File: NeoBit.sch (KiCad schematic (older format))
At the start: 19 parts, among them J1 AudioJack3_Ground, J2 Barrel_Jack_MountingPin, J3 Qwiic, J4 DotStars, J5 microbit_edge_connector, J6 NeoPixels, U1 74AHCT125, U2 MCP1702-3302E_TO92, U3 MCP1702-5002E_TO92

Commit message: Part numbers for terminal blocks.
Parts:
- J4: Description (none) -> TERM BLOCK 4POS SIDE ENT 3.5MM; Digi-Key_PN (none) -> A98038-ND; MPN (none) -> 1776275-4
- J6: Description (none) -> TERM BLOCK 3POS SIDE ENT 3.5MM; Digi-Key_PN (none) -> A98037-ND; MPN (none) -> 1776275-3
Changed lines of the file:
@@
 F 2 "footprints:TerminalBlock_4Ucon_1x03_P3.50mm_Vertical" H 6500 4800 50  0001 C CNN
 F 3 "" H 6500 4800 50  0001 C CNN
+F 4 "1776275-3" H 6500 4800 60  0001 C CNN "MPN"
+F 5 "TERM BLOCK 3POS SIDE ENT 3.5MM" H 6500 4800 60  0001 C CNN "Description"
+F 6 "A98037-ND" H 6500 4800 60  0001 C CNN "Digi-Key_PN"
 	1    6500 4800
 	1    0    0    -1
@@
 F 2 "footprints:TerminalBlock_4Ucon_1x04_P3.50mm_Vertical" H 5600 1600 50  0001 C CNN
 F 3 "" H 5600 1600 50  0001 C CNN
+F 4 "1776275-4" H 5600 1600 60  0001 C CNN "MPN"
+F 5 "TERM BLOCK 4POS SIDE ENT 3.5MM" H 5600 1600 60  0001 C CNN "Description"
+F 6 "A98038-ND" H 5600 1600 60  0001 C CNN "Digi-Key_PN"
 	1    5600 1600
 	1    0    0    -1

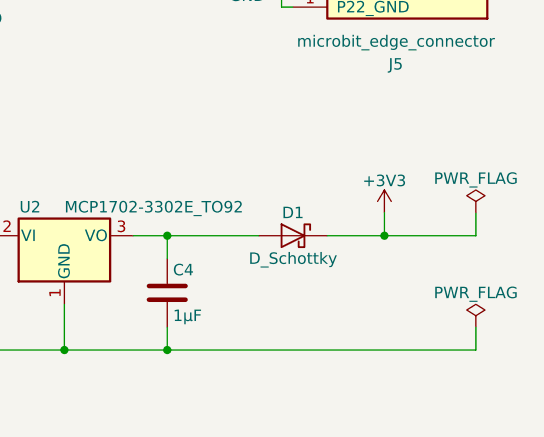
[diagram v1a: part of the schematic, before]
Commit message: Add 47uF capacitor on 3V3 supply.
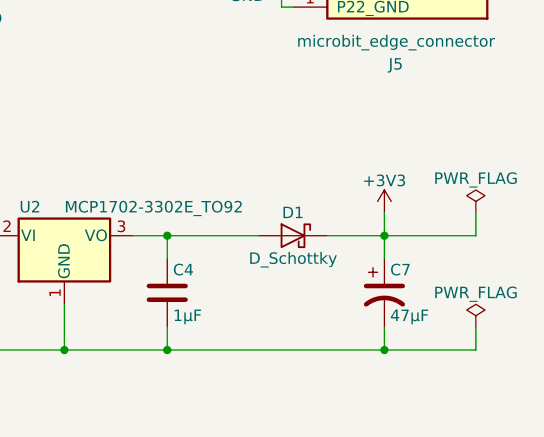
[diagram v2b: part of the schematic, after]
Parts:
- added C7: 47µF, Capacitors_THT:CP_Radial_D6.3mm_P2.50mm, symbol CP1
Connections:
- net +3V3: now also C7.1
- net GND: now also C7.2
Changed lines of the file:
@@
 NoConn ~ 7200 3500
 Wire Wire Line
-	7600 6000 7600 6100
+	7600 6000 7600 6200
 $Comp
 L +VDC #PWR018
@@
 Wire Wire Line
 	5100 4900 5350 4900
+$Comp
+L CP1 C7
+U 1 1 5B87C55E
+P 7600 6350
+F 0 "C7" H 7625 6450 50  0000 L CNN
+F 1 "47µF" H 7625 6250 50  0000 L CNN
+F 2 "Capacitors_THT:CP_Radial_D6.3mm_P2.50mm" H 7638 6200 50  0001 C CNN
+F 3 "" H 7600 6350 50  0001 C CNN
+F 4 "ECE-A1CKS470" H 7600 6350 60  0001 C CNN "MPN"
+F 5 "CAP ALUM 47UF 20% 16V RADIAL" H 7600 6350 60  0001 C CNN "Description"
+F 6 "P969-ND" H 7600 6350 60  0001 C CNN "Digi-Key_PN"
+	1    7600 6350
+	1    0    0    -1
+$EndComp
+Wire Wire Line
+	7600 6500 7600 6600
+Connection ~ 7600 6600
 $EndSCHEMATC

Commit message: Metadata.
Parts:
- J3: Description (none) -> Qwiic JST Connector - SMD 4-pin; MPN (none) -> PRT-14417
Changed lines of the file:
@@
 F 2 "Connectors_JST:JST_SH_SM04B-SRSS-TB_04x1.00mm_Angled" H 3900 1600 50  0001 C CNN
 F 3 "" H 3900 1600 50  0001 C CNN
+F 4 "PRT-14417" H 3900 1600 60  0001 C CNN "MPN"
+F 5 "Qwiic JST Connector - SMD 4-pin" H 3900 1600 60  0001 C CNN "Description"
 	1    3900 1600
 	1    0    0    -1

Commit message: Use new footprint for micro:bit edge connector.
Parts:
- J5: footprint footprints:4UCON_10156_90deg -> footprints:4UCON_10156_2x40_P1.27mm_Socket_Horizontal
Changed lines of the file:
@@
 F 0 "J5" H 7750 5350 50  0000 C CNN
 F 1 "microbit_edge_connector" H 7750 5250 50  0000 C CNN
-F 2 "footprints:4UCON_10156_90deg" H 7600 3200 50  0001 C CNN
+F 2 "footprints:4UCON_10156_2x40_P1.27mm_Socket_Horizontal" H 7600 3200 50  0001 C CNN
 F 3 "" H 7600 3200 50  0001 C CNN
 F 4 "3342" H 7700 3300 60  0001 C CNN "MPN"

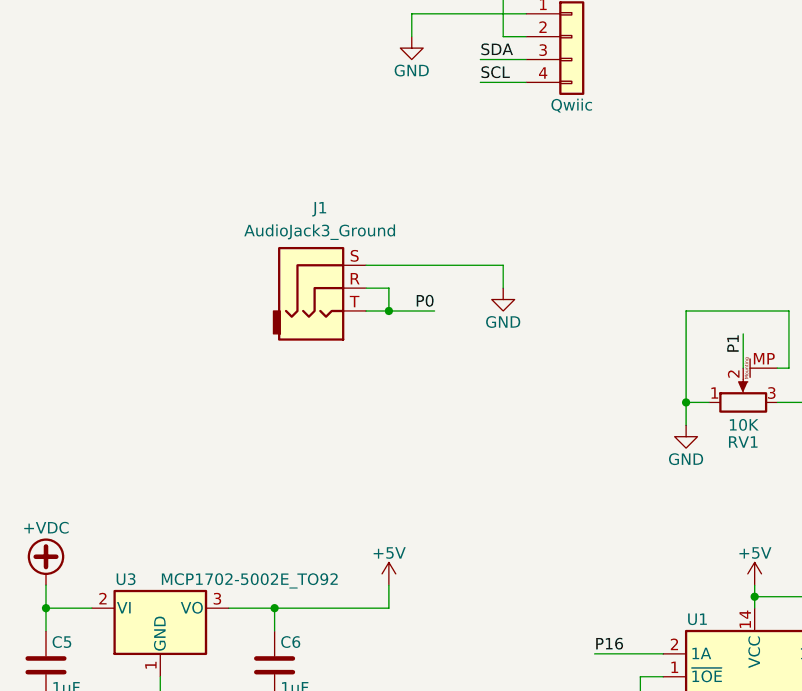
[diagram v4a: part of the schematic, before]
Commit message: Add filter to audio output.
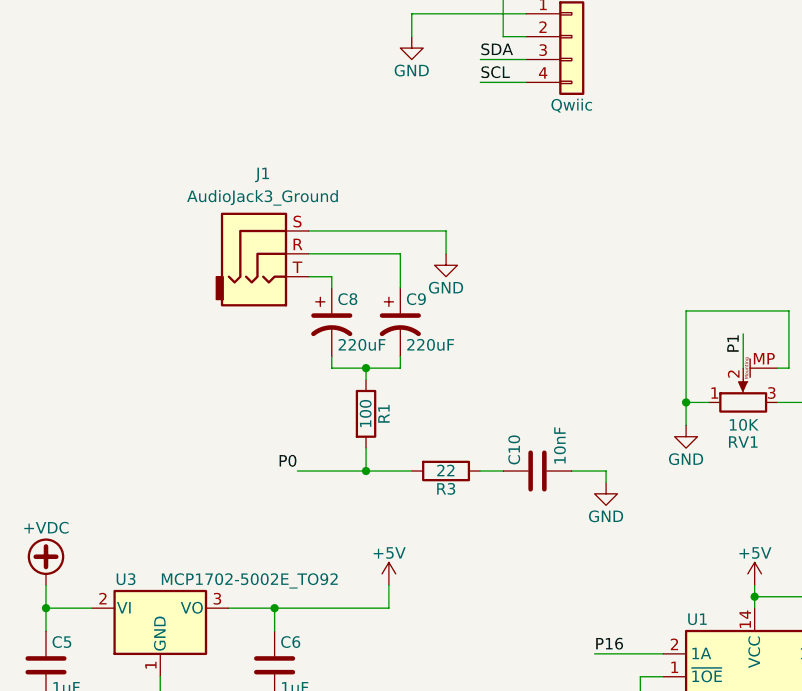
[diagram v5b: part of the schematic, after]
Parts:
- added C10: 10nF, Capacitors_THT:C_Disc_D3.8mm_W2.6mm_P2.50mm, symbol C
- added C8, C9: 220uF, Capacitors_THT:CP_Radial_D5.0mm_P2.50mm, symbol CP1
- added R1: 100, Resistors_THT:R_Axial_DIN0207_L6.3mm_D2.5mm_P2.54mm_Vertical, symbol R
- added R3: 22, Resistors_THT:R_Axial_DIN0207_L6.3mm_D2.5mm_P2.54mm_Vertical, symbol R
- R2: footprint Resistors_THT:R_Axial_DIN0207_L6.3mm_D2.5mm_P7.62mm_Horizontal -> Resistors_THT:R_Axial_DIN0207_L6.3mm_D2.5mm_P2.54mm_Vertical
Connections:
- net GND: now also C10.2
- net P0: now also R1.2, R3.2; no longer J1.R, J1.T
- new net: C9.1, J1.R
- new net: C8.1, J1.T
- new net: C8.2, C9.2, R1.1
- new net: C10.1, R3.1
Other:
- moved on the sheet: J1
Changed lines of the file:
@@
 F 0 "R2" V 5580 4550 50  0000 C CNN
 F 1 "470" V 5500 4550 50  0000 C CNN
-F 2 "Resistors_THT:R_Axial_DIN0207_L6.3mm_D2.5mm_P7.62mm_Horizontal" V 5430 4550 50  0001 C CNN
+F 2 "Resistors_THT:R_Axial_DIN0207_L6.3mm_D2.5mm_P2.54mm_Vertical" V 5430 4550 50  0001 C CNN
 F 3 "" H 5500 4550 50  0001 C CNN
 F 4 "CF14JT470R" H 5500 4550 60  0001 C CNN "MPN"
@@
 L AudioJack3_Ground J1
 U 1 1 5BA405B2
-P 2800 2700
-F 0 "J1" H 2800 3050 50  0000 C CNN
-F 1 "AudioJack3_Ground" H 2800 2950 50  0000 C CNN
-F 2 "footprints:SJ1-3533NG" H 2800 2700 50  0001 C CNN
-F 3 "" H 2800 2700 50  0001 C CNN
-F 4 "SJ1-3533NG" H 2800 2700 60  0001 C CNN "MPN"
-F 5 "CONN JACK STEREO 3.5MM R/A" H 2800 2700 60  0001 C CNN "Description"
-F 6 "CP1-3533NG-ND" H 2800 2700 60  0001 C CNN "Digi-Key_PN"
-	1    2800 2700
+P 2550 2550
+F 0 "J1" H 2550 2900 50  0000 C CNN
+F 1 "AudioJack3_Ground" H 2550 2800 50  0000 C CNN
+F 2 "footprints:SJ1-3533NG" H 2550 2550 50  0001 C CNN
+F 3 "" H 2550 2550 50  0001 C CNN
+F 4 "SJ1-3533NG" H 2550 2550 60  0001 C CNN "MPN"
+F 5 "CONN JACK STEREO 3.5MM R/A" H 2550 2550 60  0001 C CNN "Description"
+F 6 "CP1-3533NG-ND" H 2550 2550 60  0001 C CNN "Digi-Key_PN"
+	1    2550 2550
 	1    0    0    -1
 $EndComp
@@
 L GND #PWR027
 U 1 1 5BA40629
-P 3600 2700
-F 0 "#PWR027" H 3600 2450 50  0001 C CNN
-F 1 "GND" H 3600 2550 50  0000 C CNN
-F 2 "" H 3600 2700 50  0001 C CNN
-F 3 "" H 3600 2700 50  0001 C CNN
-	1    3600 2700
-	1    0    0    -1
-$EndComp
-Wire Wire Line
-	3000 2600 3600 2600
-Wire Wire Line
-	3600 2600 3600 2700
-Text Label 3300 2800 2    50   ~ 0
+P 3350 2550
+F 0 "#PWR027" H 3350 2300 50  0001 C CNN
+F 1 "GND" H 3350 2400 50  0000 C CNN
+F 2 "" H 3350 2550 50  0001 C CNN
+F 3 "" H 3350 2550 50  0001 C CNN
+	1    3350 2550
+	1    0    0    -1
+$EndComp
+Wire Wire Line
+	2750 2450 3350 2450
+Wire Wire Line
+	3350 2450 3350 2550
+Text Label 2700 3500 2    50   ~ 0
 P0
-Wire Wire Line
-	3000 2800 3300 2800
-Wire Wire Line
-	3000 2700 3100 2700
-Wire Wire Line
-	3100 2700 3100 2800
-Connection ~ 3100 2800
 Text Label 7000 3700 0    50   ~ 0
 P16
@@
 	7600 6500 7600 6600
 Connection ~ 7600 6600
+$Comp
+L CP1 C8
+U 1 1 5BA7BE4E
+P 2850 2850
+F 0 "C8" H 2875 2950 50  0000 L CNN
+F 1 "220uF" H 2875 2750 50  0000 L CNN
+F 2 "Capacitors_THT:CP_Radial_D5.0mm_P2.50mm" H 2850 2850 50  0001 C CNN
+F 3 "" H 2850 2850 50  0001 C CNN
+F 4 "UVK1A221MDD1TD" H 2850 2850 60  0001 C CNN "MPN"
+F 5 "CAP ALUM 220UF 20% 10V RADIAL" H 2850 2850 60  0001 C CNN "Description"
+F 6 "493-7455-1-ND" H 2850 2850 60  0001 C CNN "Digi-Key_PN"
+	1    2850 2850
+	1    0    0    -1
+$EndComp
+$Comp
+L CP1 C9
+U 1 1 5BA7BFBB
+P 3150 2850
+F 0 "C9" H 3175 2950 50  0000 L CNN
+F 1 "220uF" H 3175 2750 50  0000 L CNN
+F 2 "Capacitors_THT:CP_Radial_D5.0mm_P2.50mm" H 3150 2850 50  0001 C CNN
+F 3 "" H 3150 2850 50  0001 C CNN
+F 4 "UVK1A221MDD1TD" H 3150 2850 60  0001 C CNN "MPN"
+F 5 "CAP ALUM 220UF 20% 10V RADIAL" H 3150 2850 60  0001 C CNN "Description"
+F 6 "493-7455-1-ND" H 3150 2850 60  0001 C CNN "Digi-Key_PN"
+	1    3150 2850
+	1    0    0    -1
+$EndComp
+Wire Wire Line
+	2750 2650 2850 2650
+Wire Wire Line
+	2850 2650 2850 2700
+Wire Wire Line
+	2750 2550 3150 2550
+Wire Wire Line
+	3150 2550 3150 2700
+$Comp
+L R R1
+U 1 1 5BA7C192
+P 3000 3250
+F 0 "R1" V 3080 3250 50  0000 C CNN
+F 1 "100" V 3000 3250 50  0000 C CNN
+F 2 "Resistors_THT:R_Axial_DIN0207_L6.3mm_D2.5mm_P2.54mm_Vertical" V 2930 3250 50  0001 C CNN
+F 3 "" H 3000 3250 50  0001 C CNN
+	1    3000 3250
+	1    0    0    -1
+$EndComp
+$Comp
+L R R3
+U 1 1 5BA7C263
+P 3350 3500
+F 0 "R3" V 3430 3500 50  0000 C CNN
+F 1 "22" V 3350 3500 50  0000 C CNN
+F 2 "Resistors_THT:R_Axial_DIN0207_L6.3mm_D2.5mm_P2.54mm_Vertical" V 3280 3500 50  0001 C CNN
+F 3 "" H 3350 3500 50  0001 C CNN
+	1    3350 3500
+	0    1    1    0
+$EndComp
+$Comp
+L C C10
+U 1 1 5BA7C341
+P 3750 3500
+F 0 "C10" H 3775 3600 50  0000 L CNN
+F 1 "10nF" H 3775 3400 50  0000 L CNN
+F 2 "Capacitors_THT:C_Disc_D3.8mm_W2.6mm_P2.50mm" H 3788 3350 50  0001 C CNN
+F 3 "" H 3750 3500 50  0001 C CNN
+F 4 "K103K15X7RF5TL2" H 3750 3500 60  0001 C CNN "MPN"
+F 5 "CAP CER 10000PF 50V X7R RADIAL" H 3750 3500 60  0001 C CNN "Description"
+F 6 "BC1078CT-ND" H 3750 3500 60  0001 C CNN "Digi-Key_PN"
+	1    3750 3500
+	0    -1   -1   0
+$EndComp
+$Comp
+L GND #PWR028
+U 1 1 5BA7C3DA
+P 4050 3550
+F 0 "#PWR028" H 4050 3300 50  0001 C CNN
+F 1 "GND" H 4050 3400 50  0000 C CNN
+F 2 "" H 4050 3550 50  0001 C CNN
+F 3 "" H 4050 3550 50  0001 C CNN
+	1    4050 3550
+	1    0    0    -1
+$EndComp
+Wire Wire Line
+	2850 3000 2850 3050
+Wire Wire Line
+	2850 3050 3150 3050
+Wire Wire Line
+	3150 3050 3150 3000
+Wire Wire Line
+	3000 3100 3000 3050
+Connection ~ 3000 3050
+Wire Wire Line
+	2700 3500 3200 3500
+Wire Wire Line
+	3000 3400 3000 3500
+Connection ~ 3000 3500
+Wire Wire Line
+	3500 3500 3600 3500
+Wire Wire Line
+	3900 3500 4050 3500
+Wire Wire Line
+	4050 3500 4050 3550
 $EndSCHEMATC
